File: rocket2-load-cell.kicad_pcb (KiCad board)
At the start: 2 copper layers, 45 x 90 mm, 47 parts, among them J1 SWD, J3 PJ-002A, J4 Conn_01x02, J5 USB_C_Receptacle_USB2.0_14P, U1 STM32F103C8Tx, U3 LD1117V33, Y1 16MHz

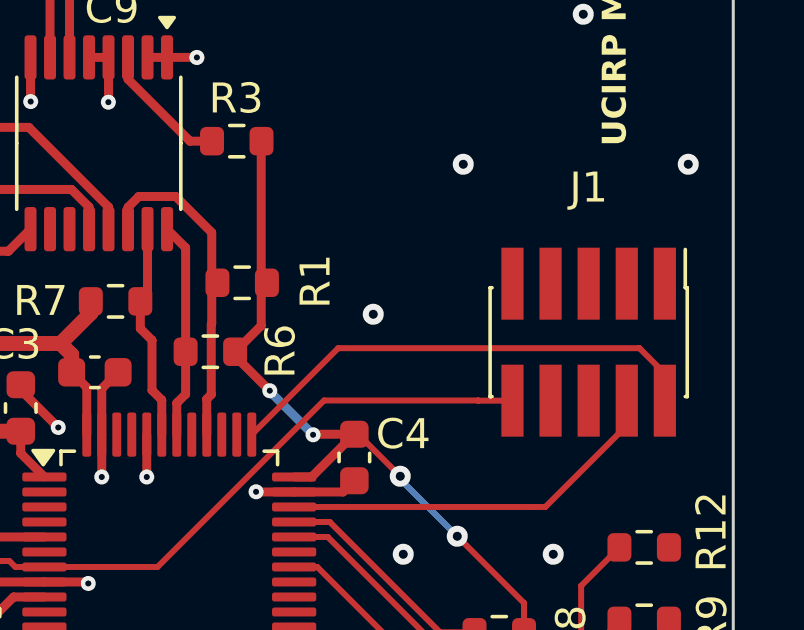
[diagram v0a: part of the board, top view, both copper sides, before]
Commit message: Final Adjustment: SWD Power
Hooked up power after adjusting layout
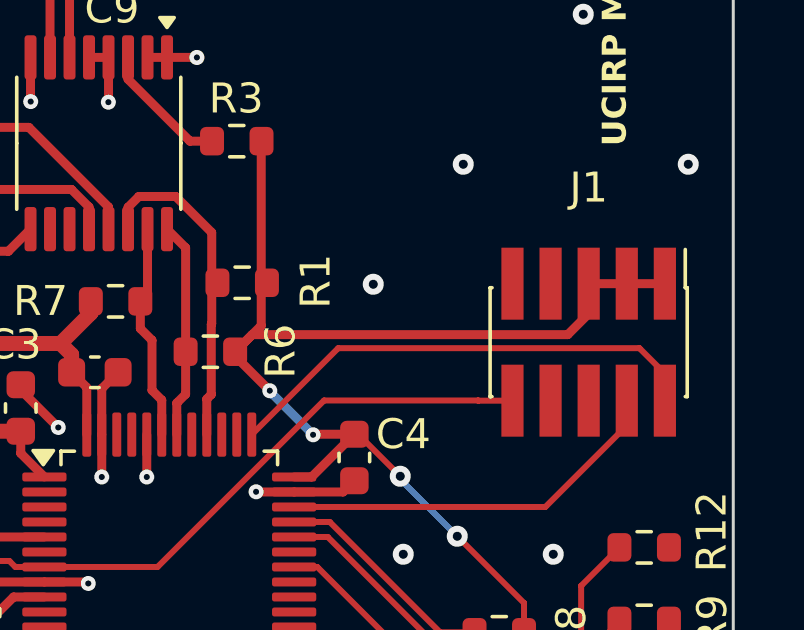
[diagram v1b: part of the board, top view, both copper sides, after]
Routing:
- net +3.3V: track 151.9 -> 167.8 mm
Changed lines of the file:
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@@
+	)
+	(segment
+		(start 150.18 89.982)
+		(end 149.483 90.679)
+		(width 0.3)
+		(layer "F.Cu")
+		(net 1)
 	)
 	(segment
@@
 	)
 	(segment
+		(start 150.18 88.98)
+		(end 150.18 89.982)
+		(width 0.3)
+		(layer "F.Cu")
+		(net 1)
+	)
+	(segment
+		(start 151.45 88.98)
+		(end 150.18 88.98)
+		(width 0.3)
+		(layer "F.Cu")
+		(net 1)
+	)
+	(segment
 		(start 122 103.7)
 		(end 122 99.48)
@@
 	)
 	(segment
+		(start 152.72 88.98)
+		(end 151.45 88.98)
+		(width 0.3)
+		(layer "F.Cu")
+		(net 1)
+	)
+	(segment
 		(start 123.65 97.05)
 		(end 123.56 97.05)
@@
 		(end 116.98 93.9)
 		(width 0.5)
+		(layer "F.Cu")
+		(net 1)
+	)
+	(segment
+		(start 149.483 90.679)
+		(end 138.96479 90.679)
+		(width 0.3)
 		(layer "F.Cu")
 		(net 1)
@@
 	)
 	(segment
+		(start 138.96479 90.679)
+		(end 138.395 91.24879)
+		(width 0.3)
+		(layer "F.Cu")
+		(net 1)
+	)
+	(segment
 		(start 122 99.48)
 		(end 121.99 99.47)
@@
 	)
 	(via
-		(at 143 90)
-		(size 0.7)
-		(drill 0.3)
+		(at 143 89)
+		(size 0.7)
+		(drill 0.3)

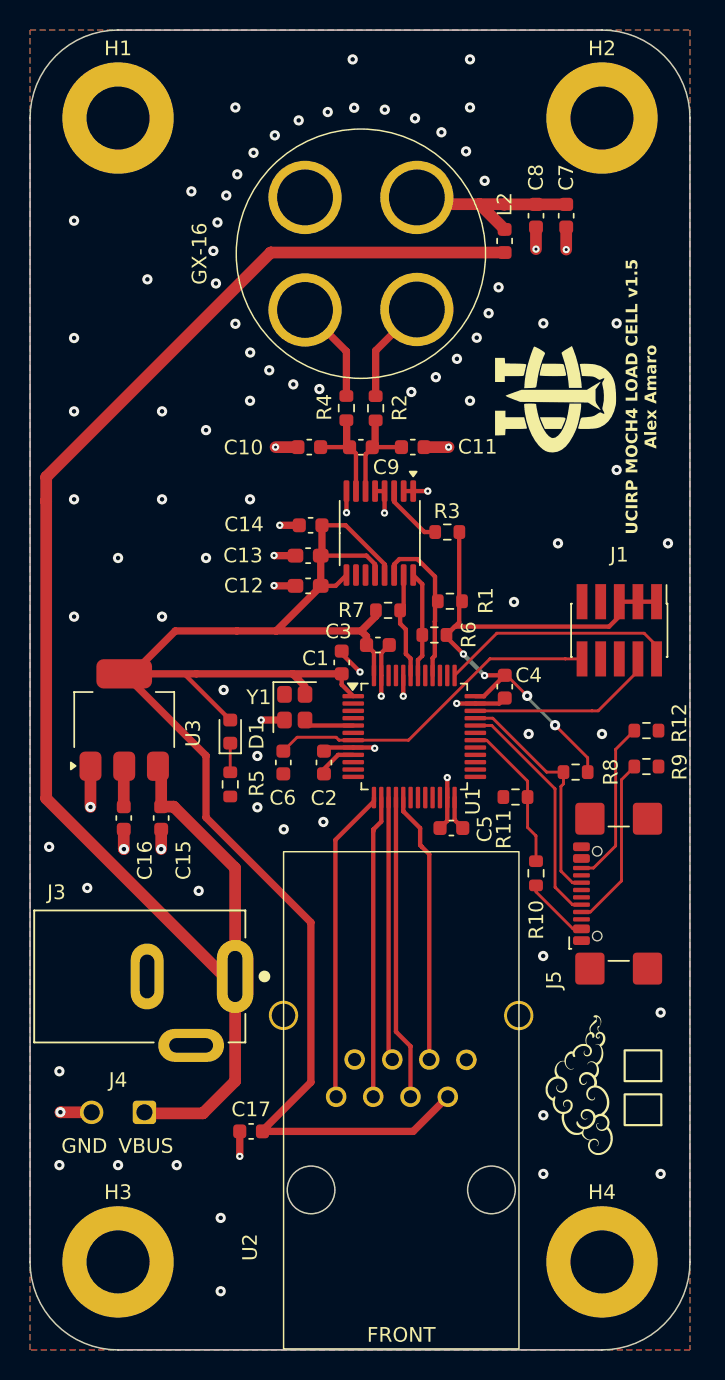
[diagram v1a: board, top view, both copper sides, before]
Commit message: LC v1.5 Fixes (Pt. 1)
Fixes shorts, pin configurations, among other vital details
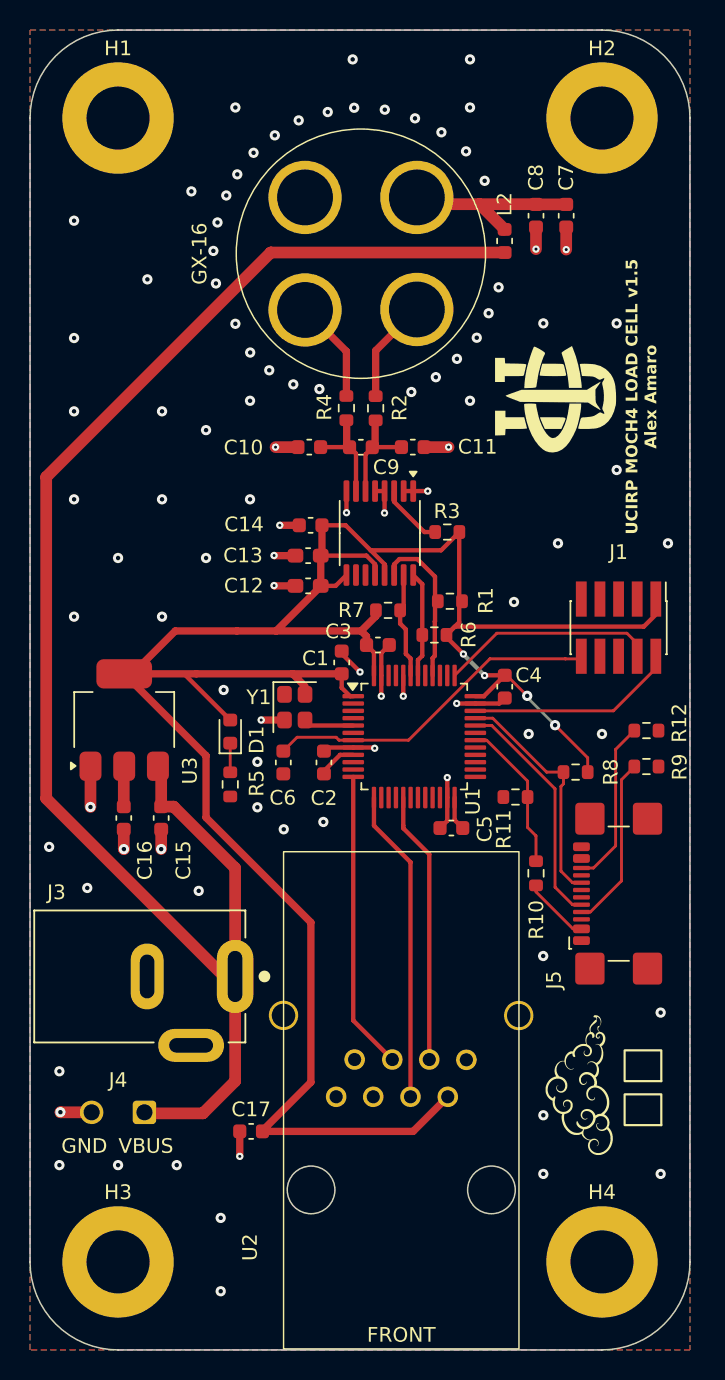
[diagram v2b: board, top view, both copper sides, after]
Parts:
- moved J1 0.19 mm to (150.1, 90.8)
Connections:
- J1 pad 3: +3.3V -> GND
- J1 pad 5: +3.3V -> GND
- U1 pad 12: unconnected-(U1-PA2-Pad12) -> ETH_TX
- U1 pad 13: ETH_CTS -> ETH_RX
- U1 pad 14: ETH_RTS -> unconnected-(U1-PA4-Pad14)
- U1 pad 15: ETH_TX -> unconnected-(U1-PA5-Pad15)
- U1 pad 16: ETH_RX -> unconnected-(U1-PA6-Pad16)
- U1 pad 34: DEBUG_SWCLK -> DEBUG_SWDIO
- U1 pad 37: DEBUG_SWDIO -> DEBUG_SWCLK
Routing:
- net ETH_CTS: track 21.5 -> 0.07 mm
- net ETH_RTS: track 20.6 -> 0.00 mm
- net +3.3V: track 167.8 -> 173.7 mm
- net DEBUG_SWCLK: track 13.0 -> 15.6 mm
- net ETH_TX: track 18.0 -> 20.4 mm
- net DEBUG_SWDIO: track 16.2 -> 14.3 mm
- net ETH_RX: track 20.8 -> 21.4 mm

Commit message: LC v1.5 Fixes (Pt. 2)
Corrected GX-16 footprint, removed vias from ADC, adjusted decap power line routing, and matched length more for ADS_CLK and ADS_DATA
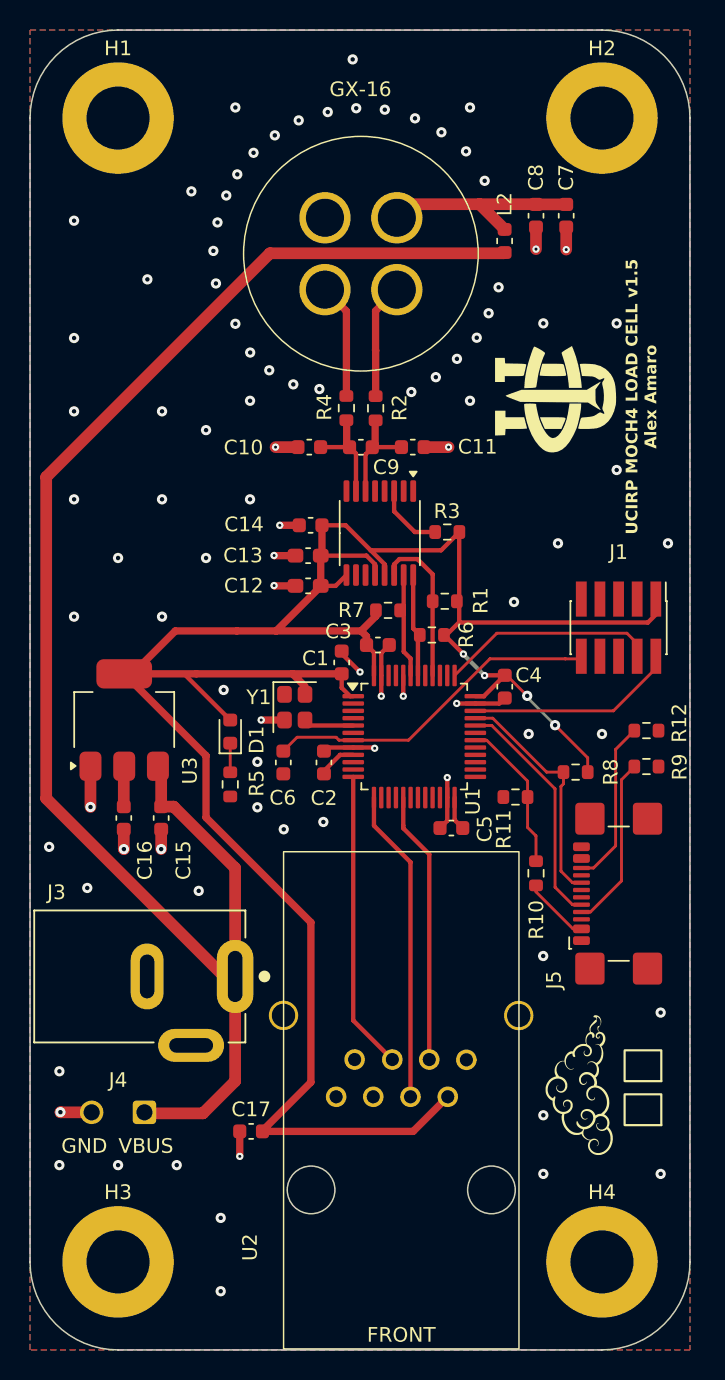
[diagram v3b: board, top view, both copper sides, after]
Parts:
- moved R1 0.35 mm to (138.3, 89.0)
- moved R6 0.17 mm to (137.4, 91.2)
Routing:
- net GND: track 45.2 -> 39.9 mm, vias 95 -> 91
- net VLC: track 16.0 -> 14.4 mm
- net +3.3V: track 173.7 -> 172.2 mm
- net AIN+: track 7.21 -> 7.89 mm
- net AIN-: track 7.27 -> 7.90 mm

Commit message: LC v1.5 Fixes (Pt. 3)
Adjusted 10V power line path and filtering on 10V power line near GX connector
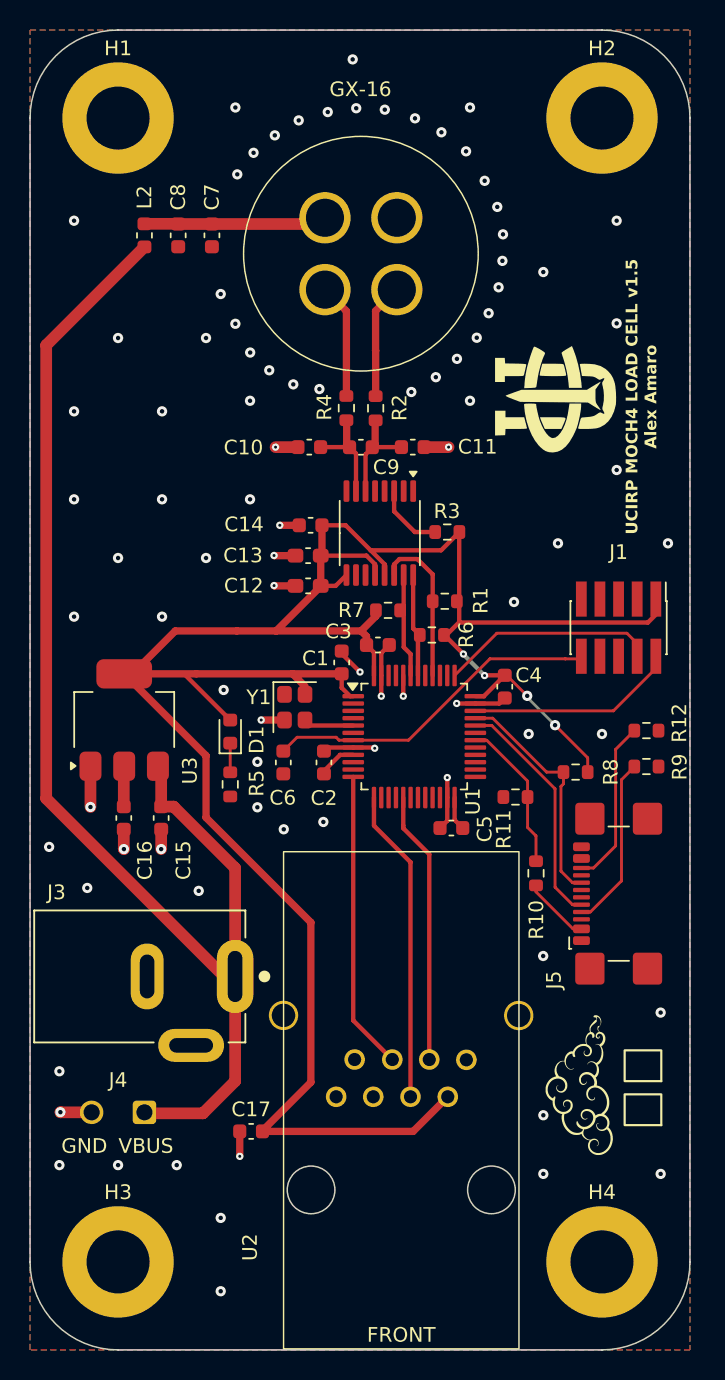
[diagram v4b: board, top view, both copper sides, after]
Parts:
- moved L2 24.6 mm to (117.8, 64.0)
- moved C8 24.4 mm to (120.1, 64.0)
- moved C7 24.2 mm to (122.4, 64.0)
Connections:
- GX-16 pad 2: VLC -> GND
- GX-16 pad 3: GND -> VLC
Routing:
- net VBUS: track 111.0 -> 91.9 mm
- net GND: track 39.9 -> 38.2 mm, vias 91 -> 88
- net VLC: track 14.4 -> 13.1 mm
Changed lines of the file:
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@@
 	(footprint "Capacitor_SMD:C_0603_1608Metric"
 		(layer "F.Cu")
-		(at 146.56 62.6625 -90)
+		(at 122.4 64 -90)
 		(descr "Capacitor SMD 0603 (1608 Metric), square (rectangular) end terminal, IPC-7351 nominal, (Body size source: IPC-SM-782 page 76, https://www.pcb-3d.com/wordpress/wp-content/uploads/ipc-sm-782a_amendment_1_and_2.pdf), generated with kicad-footprint-generator")
 		(tags "capacitor")
@@
 			(layers "*.Cu" "*.Mask")
 			(remove_unused_layers no)
-			(net 5 "VLC")
+			(net 2 "GND")
 			(pintype "input")
 		)
@@
 			(layers "*.Cu" "*.Mask")
 			(remove_unused_layers no)
-			(net 2 "GND")
+			(net 5 "VLC")
 			(pintype "input")
 		)
@@
 	(footprint "Inductor_SMD:L_0603_1608Metric"
 		(layer "F.Cu")
-		(at 142.36 64.38274 -90)
+		(at 117.8 64 -90)
 		(descr "Inductor SMD 0603 (1608 Metric), square (rectangular) end terminal, IPC-7351 nominal, (Body size source: http://www.tortai-tech.com/upload/download/2011102023233369053.pdf), generated with kicad-footprint-generator")
 		(tags "inductor")
 		(property "Reference" "L2"
-			(at -2.5125 0 90)
+			(at -2.6 0 90)
 			(layer "F.SilkS")
 			(effects
@@
 	(footprint "Capacitor_SMD:C_0603_1608Metric"
 		(layer "F.Cu")
-		(at 144.5 62.6625 -90)
+		(at 120.1 64 -90)
 		(descr "Capacitor SMD 0603 (1608 Metric), square (rectangular) end terminal, IPC-7351 nominal, (Body size source: IPC-SM-782 page 76, https://www.pcb-3d.com/wordpress/wp-content/uploads/ipc-sm-782a_amendment_1_and_2.pdf), generated with kicad-footprint-generator")
 		(tags "capacitor")
@@
 	)
 	(segment
+		(start 135.935 61.875)
+		(end 135.01 62.8)
+		(width 0.8)
+		(layer "F.Cu")
+		(net 2)
+	)
+	(segment
 		(start 127.35 97.04879)
 		(end 125.76121 97.04879)
@@
 	)
 	(segment
-		(start 146.56 63.4375)
-		(end 146.56 64.97)
-		(width 0.8)
-		(layer "F.Cu")
-		(net 2)
-	)
-	(segment
-		(start 144.5 63.4375)
-		(end 144.5 64.94)
-		(width 0.8)
-		(layer "F.Cu")
-		(net 2)
-	)
-	(segment
 		(start 134.495 91.93379)
 		(end 133.95 92.47879)
@@
 	)
 	(via
-		(at 121 61)
-		(size 0.7)
-		(drill 0.3)
-		(layers "F.Cu" "B.Cu")
-		(free yes)
-		(net 2)
-	)
-	(via
 		(at 125.24 58.36976)
 		(size 0.7)
@@
 	)
 	(via
-		(at 122 77.27976)
+		(at 122 71)
 		(size 0.7)
 		(drill 0.3)
@@
 	)
 	(via
-		(at 123.38 61.27976)
+		(at 141.86 62.06)
 		(size 0.7)
 		(drill 0.3)
@@
 	)
 	(via
-		(at 122.78 63.11976)
+		(at 142.25 63.93)
 		(size 0.7)
 		(drill 0.3)
@@
 	)
 	(via
-		(at 122.675 67.27976)
+		(at 123 68)
 		(size 0.7)
 		(drill 0.3)
@@
 	)
 	(via
-		(at 146.56 64.97)
-		(size 0.5)
-		(drill 0.2)
-		(layers "F.Cu" "B.Cu")
-		(net 2)
-	)
-	(via
-		(at 118 67)
-		(size 0.7)
-		(drill 0.3)
-		(layers "F.Cu" "B.Cu")
-		(free yes)
-		(net 2)
-	)
-	(via
 		(at 111.3 105.7)
 		(size 0.7)
@@
 	)
 	(via
-		(at 113 71)
+		(at 116 71)
 		(size 0.7)
 		(drill 0.3)
@@
 	)
 	(via
-		(at 122.5 65.05976)
+		(at 142.21 65.74)
 		(size 0.7)
 		(drill 0.3)
@@
 	)
 	(via
-		(at 144.5 64.94)
-		(size 0.5)
-		(drill 0.2)
-		(layers "F.Cu" "B.Cu")
-		(net 2)
-	)
-	(via
 		(at 139.73 58.26976)
 		(size 0.7)
@@
 	)
 	(via
-		(at 145 70)
+		(at 145 66.5)
 		(size 0.7)
 		(drill 0.3)
@@
 	)
 	(via
+		(at 150 63)
+		(size 0.7)
+		(drill 0.3)
+		(layers "F.Cu" "B.Cu")
+		(free yes)
+		(net 2)
+	)
+	(via
 		(at 140 55.27976)
 		(size 0.7)
@@
 	)
 	(segment
-		(start 111.1 102.4)
-		(end 111.1 80.47976)
+		(start 118.89 100.2)
+		(end 118.72 100.2)
 		(width 0.8)
 		(layer "F.Cu")
@@
 	)
 	(segment
-		(start 118.89 100.2)
-		(end 118.72 100.2)
+		(start 117.8 64.7875)
+		(end 111.1 71.4875)
 		(width 0.8)
 		(layer "F.Cu")
@@
 	)
 	(segment
-		(start 123.235 114.535)
-		(end 111.1 102.4)
-		(width 0.8)
-		(layer "F.Cu")
-		(net 4)
-	)
-	(segment
-		(start 123.9825 114.535)
-		(end 123.235 114.535)
-		(width 0.8)
-		(layer "F.Cu")
-		(net 4)
-	)
-	(segment
 		(start 123.9825 121.6775)
 		(end 123.9825 114.535)
@@
 	)
 	(segment
-		(start 111.1 80.47976)
-		(end 126.35976 65.22)
-		(width 0.8)
-		(layer "F.Cu")
-		(net 4)
-	)
-	(segment
-		(start 126.35976 65.22)
-		(end 142.31024 65.22)
-		(width 0.8)
-		(layer "F.Cu")
-		(net 4)
-	)
-	(segment
 		(start 123.9825 116.5825)
 		(end 123.9825 114.535)
@@
 	)
 	(segment
-		(start 142.31024 65.22)
-		(end 142.36 65.17024)
+		(start 119.795 102.955)
+		(end 118.94 102.955)
 		(width 0.8)
 		(layer "F.Cu")
@@
 	)
 	(segment
-		(start 119.795 102.955)
-		(end 118.94 102.955)
+		(start 111.1 102.4)
+		(end 123.235 114.535)
 		(width 0.8)
 		(layer "F.Cu")
@@
 	)
 	(segment
+		(start 111.1 71.4875)
+		(end 111.1 102.4)
+		(width 0.8)
+		(layer "F.Cu")
+		(net 4)
+	)
+	(segment
 		(start 123.9825 107.1425)
 		(end 119.795 102.955)
@@
 	)
 	(segment
-		(start 144.4875 61.875)
-		(end 140.65 61.875)
+		(start 123.235 114.535)
+		(end 123.9825 114.535)
 		(width 0.8)
 		(layer "F.Cu")
-		(net 5)
+		(net 4)
 	)
 	(segment
-		(start 144.5 61.8875)
-		(end 146.56 61.8875)
+		(start 129.685 63.225)
+		(end 130.11 62.8)
 		(width 0.8)
 		(layer "F.Cu")
@@
 	)
 	(segment
-		(start 142.36 63.585)
-		(end 140.65 61.875)
+		(start 117.8 63.2125)
+		(end 120.0875 63.2125)
 		(width 0.8)
 		(layer "F.Cu")
@@
 	)
 	(segment
-		(start 142.3 63.625)
-		(end 142.3 63.61476)
+		(start 120.0875 63.2125)
+		(end 120.1 63.225)
 		(width 0.8)
 		(layer "F.Cu")
@@
 	)
 	(segment
-		(start 135.935 61.875)
-		(end 135.01 62.8)
+		(start 129.665 63.245)
+		(end 130.11 62.8)
 		(width 0.8)
 		(layer "F.Cu")
@@
 	)
 	(segment
-		(start 144.5 61.8875)
-		(end 144.4875 61.875)
+		(start 120.1 63.225)
+		(end 122.4 63.225)
 		(width 0.8)
 		(layer "F.Cu")
@@
 	)
 	(segment
-		(start 140.65 61.875)
-		(end 135.935 61.875)
+		(start 122.4 63.225)
+		(end 129.685 63.225)
 		(width 0.8)
 		(layer "F.Cu")
@@
 	)
 	(segment
-		(start 135.95 92.86)
-		(end 135.48 92.39)
+		(start 135.95 94.01129)
+		(end 135.95 92.55)
 		(width 0.3)
 		(layer "F.Cu")
@@
 	)
 	(segment
-		(start 135.48 92.39)
+		(start 135.48 92.08)
 		(end 135.48 89.815)
 		(width 0.3)
@@
 	)
 	(segment
-		(start 135.95 94.01129)
-		(end 135.95 92.86)
-		(width 0.3)
-		(layer "F.Cu")
-		(net 37)
-	)
-	(segment
 		(start 135.48 89.815)
 		(end 135.235 89.57)
@@
 		(width 0.3)
 		(layer "F.Cu")
+		(net 37)
+	)
+	(segment
+		(start 135.95 92.55)
+		(end 135.48 92.08)
+		(width 0.3)
+		(layer "F.Cu")

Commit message: LC v1.5 (Pt. 4)
Final routing changes
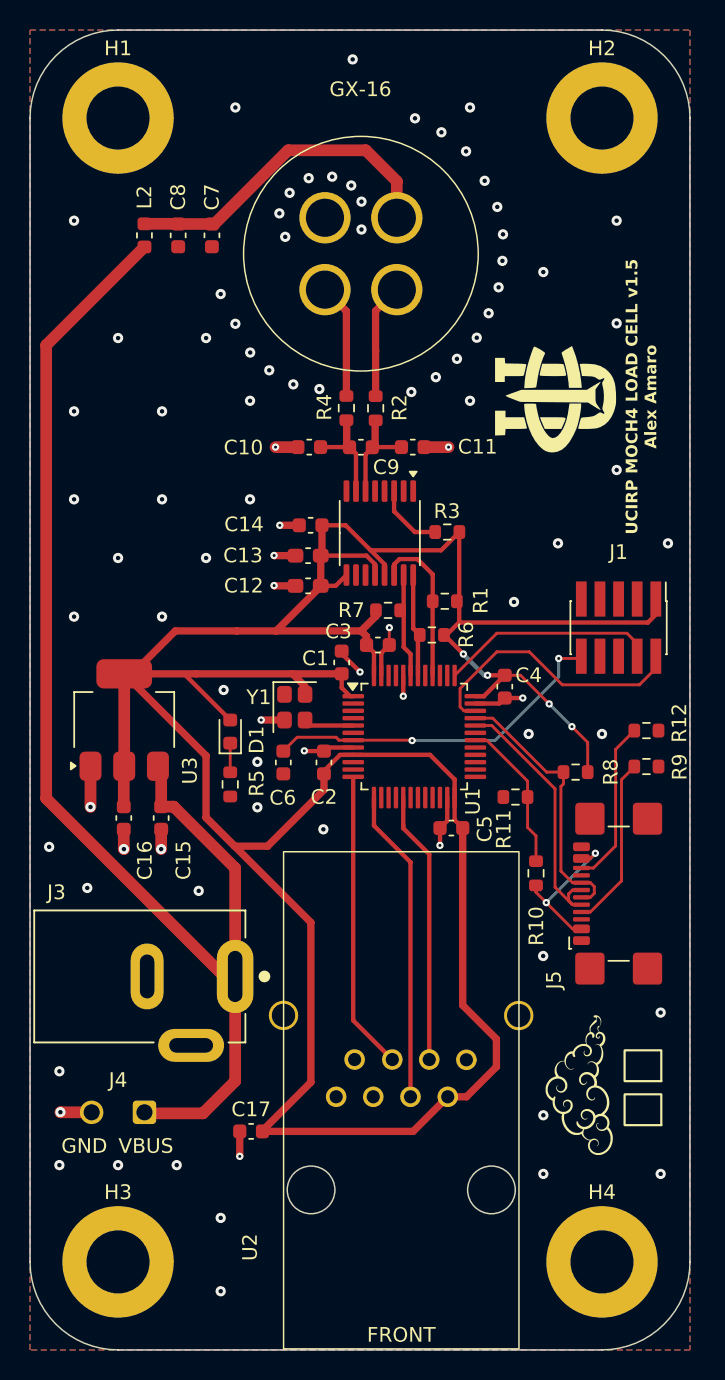
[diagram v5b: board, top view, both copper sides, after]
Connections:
- GX-16 pad 2: GND -> VLC
- GX-16 pad 3: VLC -> GND
- J5 pad A6: unconnected-(J5-D+-PadA6) -> USB_D+
- J5 pad A7: unconnected-(J5-D--PadA7) -> USB_D-
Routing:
- net +3.3V: track 172.2 -> 220.9 mm
- net VLC: track 13.1 -> 24.0 mm
- net USB_VBUS: track 4.59 -> 10.5 mm, vias 0 -> 2
- net DEBUG_SWDIO: track 14.3 -> 19.0 mm
- net USB_D+: track 16.1 -> 18.5 mm
- net USB_D-: track 16.2 -> 18.1 mm
- net NRST: track 23.1 -> 23.9 mm, vias 0 -> 2
- net GND: track 38.2 -> 37.5 mm
